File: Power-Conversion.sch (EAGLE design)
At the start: 48 parts, among them Q1 SUM90P10-19L, U7 LM2678

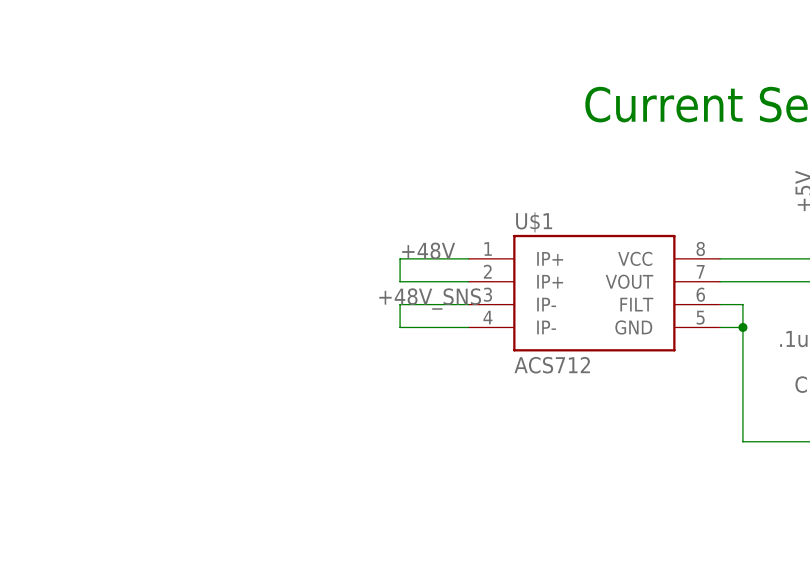
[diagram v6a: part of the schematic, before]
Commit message: Moved around parts to near final postions.  Next comes routing.
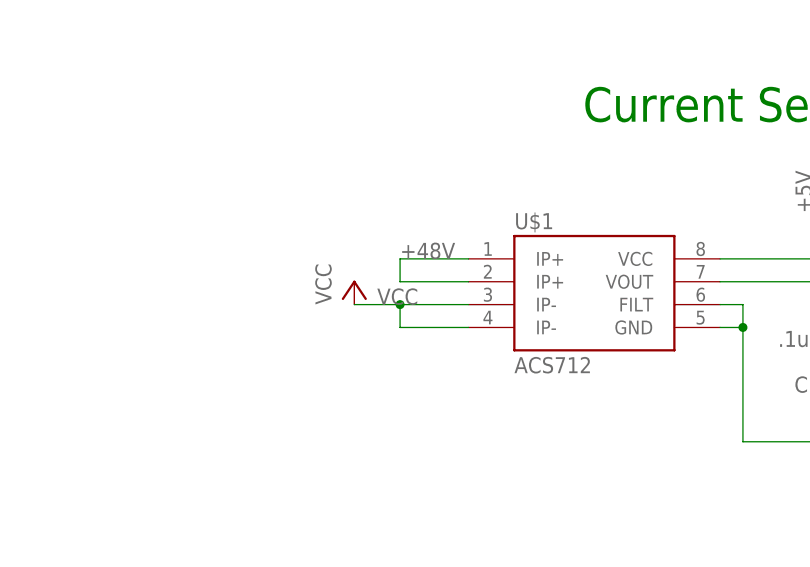
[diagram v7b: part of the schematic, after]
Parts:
- added U$15: POWER_DIST_TO_ESC, MotherBoardParts2:POWER_DIST_TO_ESC
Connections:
- removed net +48V_SNS: U$1.IP-@3, U$1.IP-@4
- net VCC: now also U$1.IP-@3, U$1.IP-@4
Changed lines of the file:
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@@
 <part name="U$13" library="MotherBoardParts2" deviceset="POWER_BRICK_CONNECTORS(2X15)" device=""/>
 <part name="U$14" library="MotherBoardParts2" deviceset="POWER_BRICK_CONNECTORS(2X15)" device=""/>
+<part name="U$15" library="MotherBoardParts2" deviceset="POWER_DIST_TO_ESC" device=""/>
+<part name="P+17" library="supply1" library_urn="urn:adsk.eagle:library:371" deviceset="VCC" device=""/>
 </parts>
 <sheets>
@@
 <instance part="U$13" gate="G$1" x="276.86" y="91.44"/>
 <instance part="U$14" gate="G$1" x="312.42" y="91.44"/>
+<instance part="P+17" gate="VCC" x="119.38" y="111.76"/>
 </instances>
 <busses>
@@
 </segment>
 </net>
-<net name="+48V_SNS" class="0">
+<net name="+12V_1" class="0">
+<segment>
+<pinref part="U$2" gate="G$1" pin="IN2"/>
+<wire x1="53.34" y1="434.34" x2="53.34" y2="424.18" width="0.1524" layer="91"/>
+<label x="53.34" y="424.18" size="1.778" layer="95"/>
+</segment>
+<segment>
+<pinref part="U$20" gate="G$1" pin="+12V"/>
+<wire x1="35.56" y1="497.84" x2="30.48" y2="497.84" width="0.1524" layer="91"/>
+<label x="30.48" y="502.92" size="1.778" layer="95"/>
+</segment>
+</net>
+<net name="+12V_2" class="0">
+<segment>
+<pinref part="U$18" gate="G$1" pin="IN2"/>
+<wire x1="142.24" y1="429.26" x2="142.24" y2="421.64" width="0.1524" layer="91"/>
+<label x="142.24" y="421.64" size="1.778" layer="95"/>
+</segment>
+<segment>
+<pinref part="U$21" gate="G$1" pin="+12V"/>
+<wire x1="124.46" y1="497.84" x2="119.38" y2="497.84" width="0.1524" layer="91"/>
+<label x="119.38" y="502.92" size="1.778" layer="95"/>
+</segment>
+</net>
+<net name="+12V_3" class="0">
+<segment>
+<pinref part="U$19" gate="G$1" pin="IN2"/>
+<wire x1="233.68" y1="429.26" x2="233.68" y2="421.64" width="0.1524" layer="91"/>
+<label x="233.68" y="424.18" size="1.778" layer="95"/>
+</segment>
+<segment>
+<pinref part="U$22" gate="G$1" pin="+12V"/>
+<wire x1="218.44" y1="497.84" x2="213.36" y2="497.84" width="0.1524" layer="91"/>
+<label x="213.36" y="502.92" size="1.778" layer="95"/>
+</segment>
+</net>
+<net name="+12V_4" class="0">
+<segment>
+<pinref part="U$24" gate="G$1" pin="IN2"/>
+<wire x1="320.04" y1="429.26" x2="320.04" y2="419.1" width="0.1524" layer="91"/>
+<label x="320.04" y="419.1" size="1.778" layer="95"/>
+</segment>
+<segment>
+<pinref part="U$23" gate="G$1" pin="+12V"/>
+<wire x1="304.8" y1="497.84" x2="299.72" y2="497.84" width="0.1524" layer="91"/>
+<label x="299.72" y="502.92" size="1.778" layer="95"/>
+</segment>
+</net>
+<net name="V-" class="0">
+<segment>
+<pinref part="U$20" gate="G$1" pin="48V_GND"/>
+<wire x1="68.58" y1="492.76" x2="73.66" y2="492.76" width="0.1524" layer="91"/>
+<pinref part="P-7" gate="1" pin="V-"/>
+</segment>
+<segment>
+<pinref part="U$21" gate="G$1" pin="48V_GND"/>
+<wire x1="157.48" y1="492.76" x2="162.56" y2="492.76" width="0.1524" layer="91"/>
+<pinref part="P-8" gate="1" pin="V-"/>
+</segment>
+<segment>
+<pinref part="U$22" gate="G$1" pin="48V_GND"/>
+<wire x1="251.46" y1="492.76" x2="256.54" y2="492.76" width="0.1524" layer="91"/>
+<pinref part="P-9" gate="1" pin="V-"/>
+</segment>
+<segment>
+<pinref part="U$23" gate="G$1" pin="48V_GND"/>
+<wire x1="337.82" y1="492.76" x2="342.9" y2="492.76" width="0.1524" layer="91"/>
+<pinref part="P-10" gate="1" pin="V-"/>
+</segment>
+</net>
+<net name="VCC" class="0">
+<segment>
+<pinref part="U$20" gate="G$1" pin="+48V"/>
+<wire x1="68.58" y1="497.84" x2="73.66" y2="497.84" width="0.1524" layer="91"/>
+<pinref part="P+6" gate="VCC" pin="VCC"/>
+</segment>
+<segment>
+<pinref part="U$21" gate="G$1" pin="+48V"/>
+<wire x1="157.48" y1="497.84" x2="162.56" y2="497.84" width="0.1524" layer="91"/>
+<pinref part="P+10" gate="VCC" pin="VCC"/>
+</segment>
+<segment>
+<pinref part="U$23" gate="G$1" pin="+48V"/>
+<wire x1="337.82" y1="497.84" x2="342.9" y2="497.84" width="0.1524" layer="91"/>
+<pinref part="P+11" gate="VCC" pin="VCC"/>
+</segment>
+<segment>
+<pinref part="U$22" gate="G$1" pin="+48V"/>
+<wire x1="251.46" y1="497.84" x2="256.54" y2="497.84" width="0.1524" layer="91"/>
+<pinref part="P+12" gate="VCC" pin="VCC"/>
+</segment>
 <segment>
 <pinref part="U$1" gate="G$1" pin="IP-@3"/>
@@
 <wire x1="124.46" y1="106.68" x2="132.08" y2="106.68" width="0.1524" layer="91"/>
 <label x="121.92" y="109.22" size="1.778" layer="95"/>
-</segment>
-</net>
-<net name="+12V_1" class="0">
-<segment>
-<pinref part="U$2" gate="G$1" pin="IN2"/>
-<wire x1="53.34" y1="434.34" x2="53.34" y2="424.18" width="0.1524" layer="91"/>
-<label x="53.34" y="424.18" size="1.778" layer="95"/>
-</segment>
-<segment>
-<pinref part="U$20" gate="G$1" pin="+12V"/>
-<wire x1="35.56" y1="497.84" x2="30.48" y2="497.84" width="0.1524" layer="91"/>
-<label x="30.48" y="502.92" size="1.778" layer="95"/>
-</segment>
-</net>
-<net name="+12V_2" class="0">
-<segment>
-<pinref part="U$18" gate="G$1" pin="IN2"/>
-<wire x1="142.24" y1="429.26" x2="142.24" y2="421.64" width="0.1524" layer="91"/>
-<label x="142.24" y="421.64" size="1.778" layer="95"/>
-</segment>
-<segment>
-<pinref part="U$21" gate="G$1" pin="+12V"/>
-<wire x1="124.46" y1="497.84" x2="119.38" y2="497.84" width="0.1524" layer="91"/>
-<label x="119.38" y="502.92" size="1.778" layer="95"/>
-</segment>
-</net>
-<net name="+12V_3" class="0">
-<segment>
-<pinref part="U$19" gate="G$1" pin="IN2"/>
-<wire x1="233.68" y1="429.26" x2="233.68" y2="421.64" width="0.1524" layer="91"/>
-<label x="233.68" y="424.18" size="1.778" layer="95"/>
-</segment>
-<segment>
-<pinref part="U$22" gate="G$1" pin="+12V"/>
-<wire x1="218.44" y1="497.84" x2="213.36" y2="497.84" width="0.1524" layer="91"/>
-<label x="213.36" y="502.92" size="1.778" layer="95"/>
-</segment>
-</net>
-<net name="+12V_4" class="0">
-<segment>
-<pinref part="U$24" gate="G$1" pin="IN2"/>
-<wire x1="320.04" y1="429.26" x2="320.04" y2="419.1" width="0.1524" layer="91"/>
-<label x="320.04" y="419.1" size="1.778" layer="95"/>
-</segment>
-<segment>
-<pinref part="U$23" gate="G$1" pin="+12V"/>
-<wire x1="304.8" y1="497.84" x2="299.72" y2="497.84" width="0.1524" layer="91"/>
-<label x="299.72" y="502.92" size="1.778" layer="95"/>
-</segment>
-</net>
-<net name="V-" class="0">
-<segment>
-<pinref part="U$20" gate="G$1" pin="48V_GND"/>
-<wire x1="68.58" y1="492.76" x2="73.66" y2="492.76" width="0.1524" layer="91"/>
-<pinref part="P-7" gate="1" pin="V-"/>
-</segment>
-<segment>
-<pinref part="U$21" gate="G$1" pin="48V_GND"/>
-<wire x1="157.48" y1="492.76" x2="162.56" y2="492.76" width="0.1524" layer="91"/>
-<pinref part="P-8" gate="1" pin="V-"/>
-</segment>
-<segment>
-<pinref part="U$22" gate="G$1" pin="48V_GND"/>
-<wire x1="251.46" y1="492.76" x2="256.54" y2="492.76" width="0.1524" layer="91"/>
-<pinref part="P-9" gate="1" pin="V-"/>
-</segment>
-<segment>
-<pinref part="U$23" gate="G$1" pin="48V_GND"/>
-<wire x1="337.82" y1="492.76" x2="342.9" y2="492.76" width="0.1524" layer="91"/>
-<pinref part="P-10" gate="1" pin="V-"/>
-</segment>
-</net>
-<net name="VCC" class="0">
-<segment>
-<pinref part="U$20" gate="G$1" pin="+48V"/>
-<wire x1="68.58" y1="497.84" x2="73.66" y2="497.84" width="0.1524" layer="91"/>
-<pinref part="P+6" gate="VCC" pin="VCC"/>
-</segment>
-<segment>
-<pinref part="U$21" gate="G$1" pin="+48V"/>
-<wire x1="157.48" y1="497.84" x2="162.56" y2="497.84" width="0.1524" layer="91"/>
-<pinref part="P+10" gate="VCC" pin="VCC"/>
-</segment>
-<segment>
-<pinref part="U$23" gate="G$1" pin="+48V"/>
-<wire x1="337.82" y1="497.84" x2="342.9" y2="497.84" width="0.1524" layer="91"/>
-<pinref part="P+11" gate="VCC" pin="VCC"/>
-</segment>
-<segment>
-<pinref part="U$22" gate="G$1" pin="+48V"/>
-<wire x1="251.46" y1="497.84" x2="256.54" y2="497.84" width="0.1524" layer="91"/>
-<pinref part="P+12" gate="VCC" pin="VCC"/>
-</segment>
-</net>
+<pinref part="P+17" gate="VCC" pin="VCC"/>
+<wire x1="124.46" y1="109.22" x2="119.38" y2="109.22" width="0.1524" layer="91"/>
+<junction x="124.46" y="109.22"/>
+</segment>
+</net>

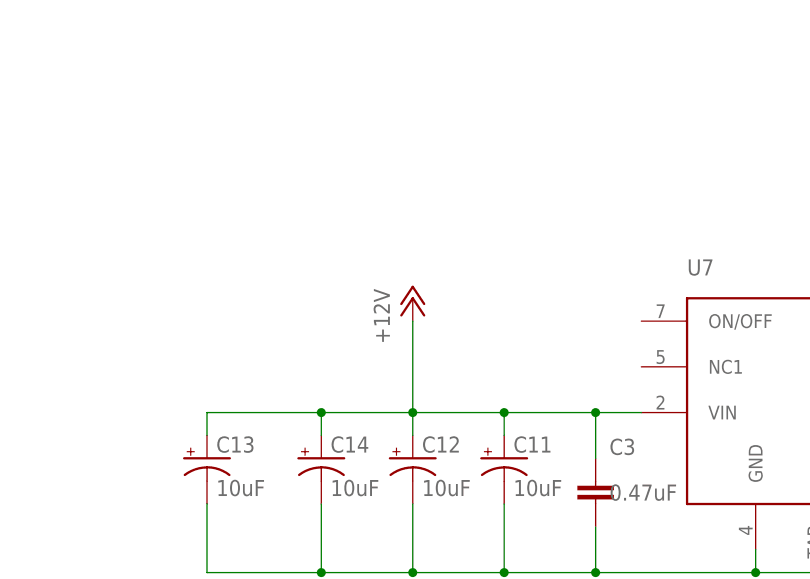
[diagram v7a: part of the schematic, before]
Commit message: Added fuse to 12V going to rasp pi
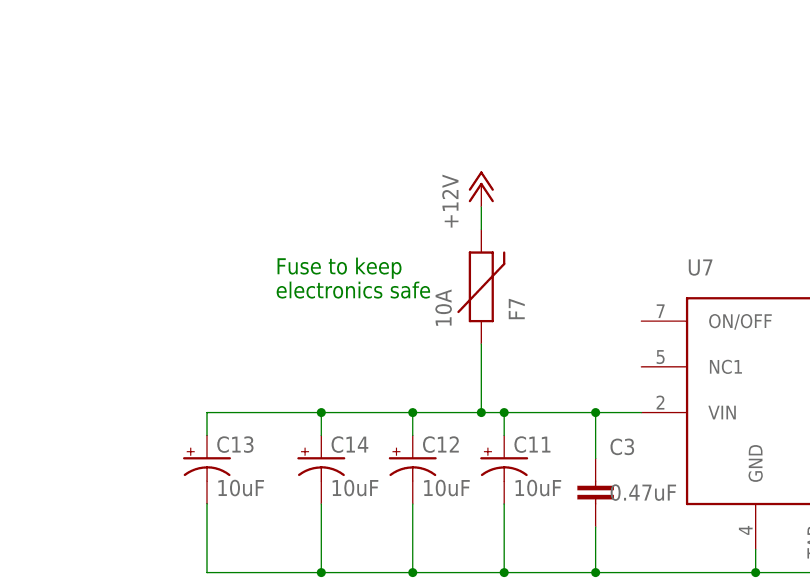
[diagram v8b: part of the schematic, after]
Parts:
- removed U$15: POWER_DIST_TO_ESC, MotherBoardParts2:POWER_DIST_TO_ESC
- added F7: 10A, PowerComponents:PTC(2920L)
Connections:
- new net N$1: C11.+, C12.+, C13.+, C14.+, C3.1, F7.1, U7.VIN
- net +12V: now also F7.2; no longer C11.+, C12.+, C13.+, C14.+, C3.1, U7.VIN
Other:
- note added: "Fuse to keep electronics safe"
